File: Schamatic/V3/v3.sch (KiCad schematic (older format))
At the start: 29 parts, among them J1 SWD, J2 SENSOR, J3 CAN, Q1 PSMN014-40YS, Q2 PSMN014-40YS, Q3 PSMN014-40YS, Q4 PSMN014-40YS, Q5 PSMN014-40YS, Q6 PSMN014-40YS, U1 STSPIN32F0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

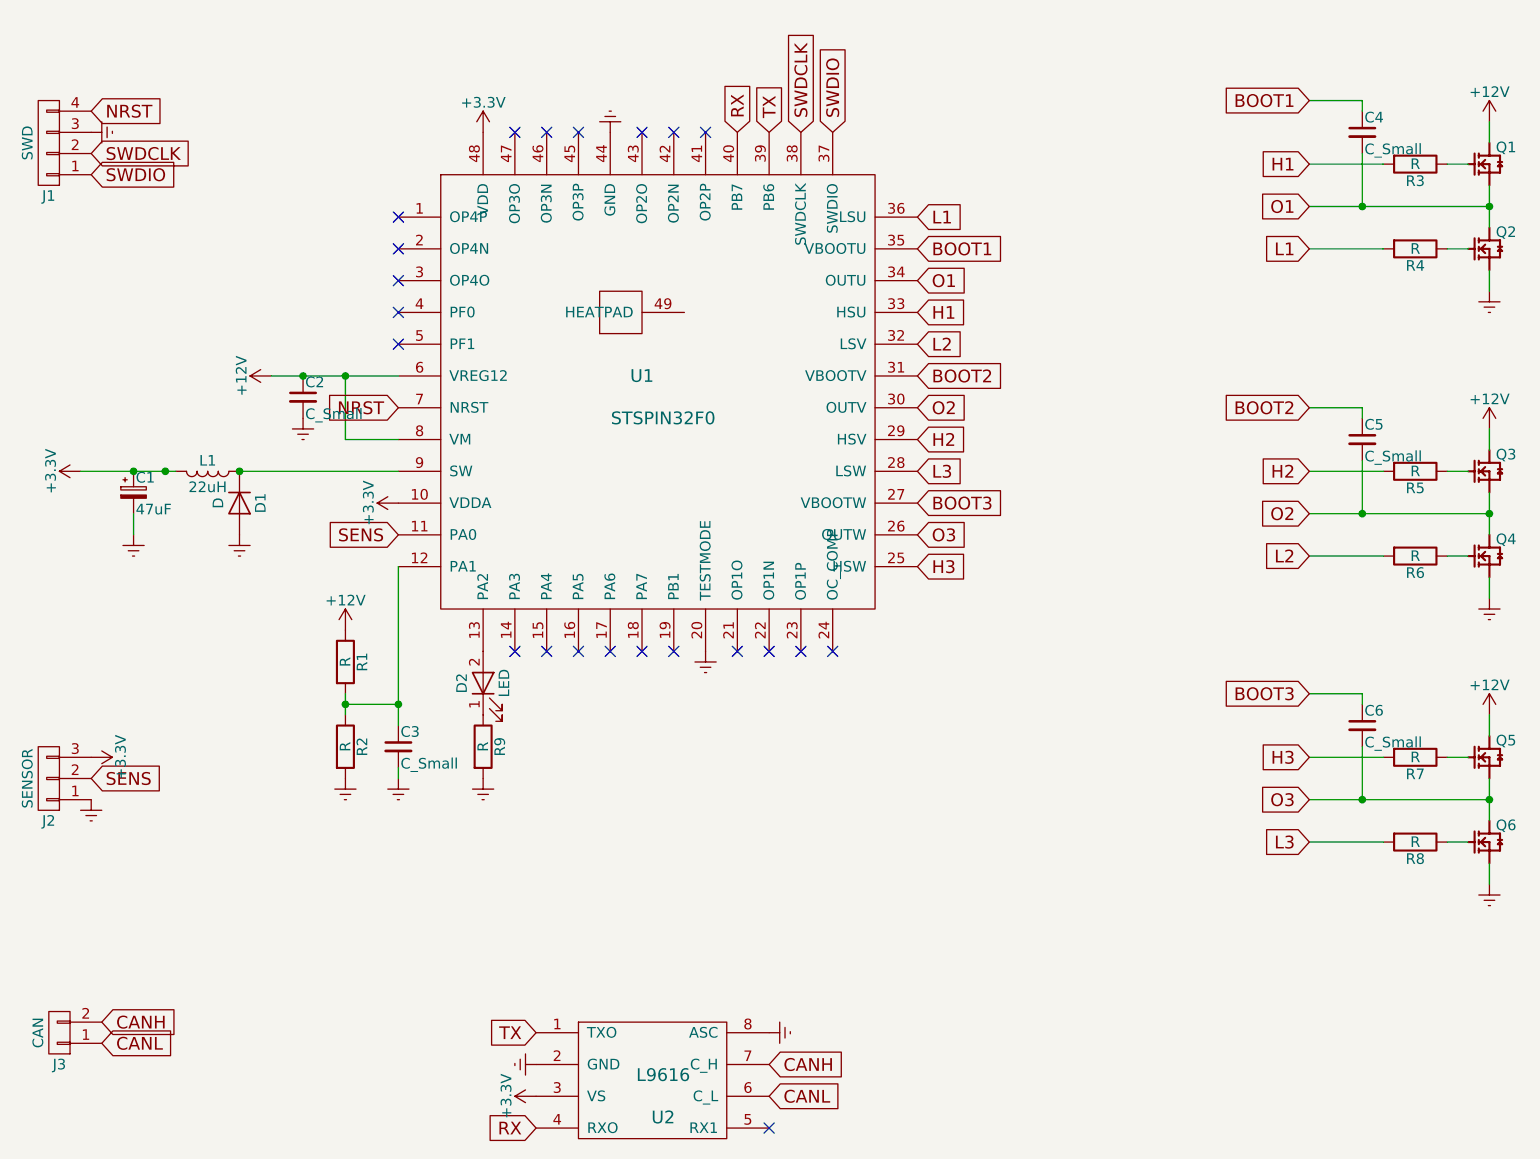
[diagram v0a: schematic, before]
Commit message: board ordered
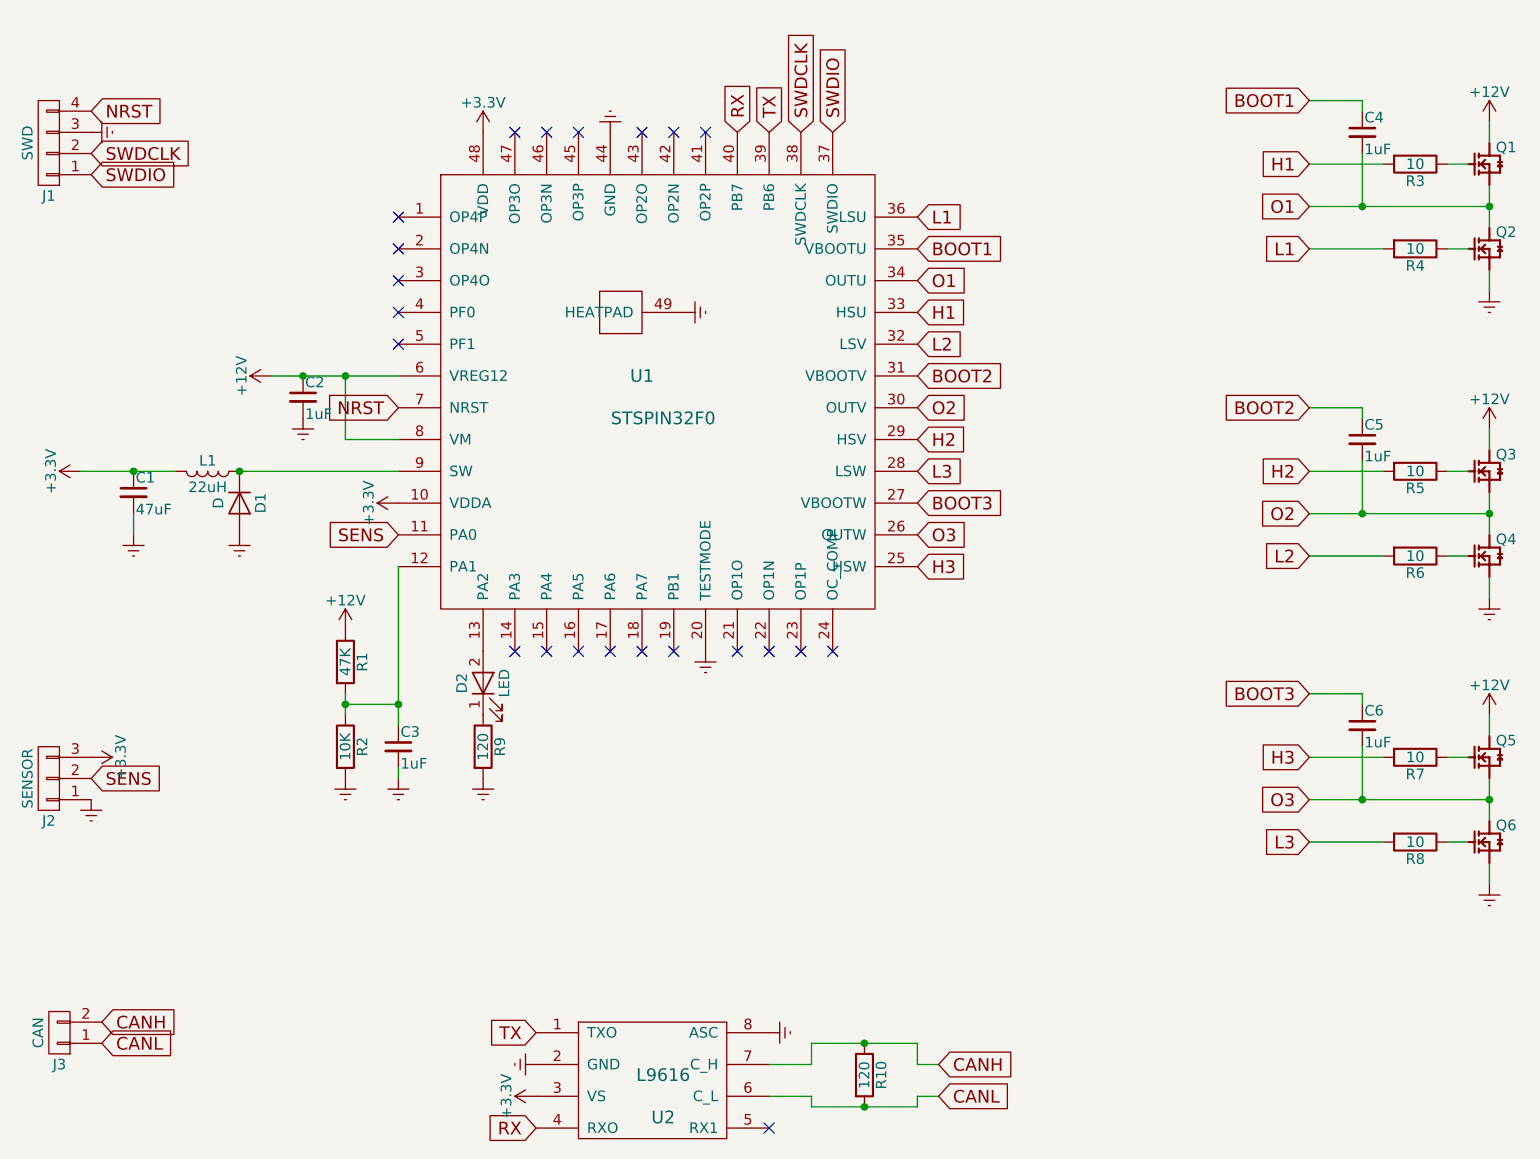
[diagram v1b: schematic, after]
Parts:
- removed C1: 47uF, Capacitors_SMD:CP_Elec_4x4.5, symbol CP_Small
- added C1: 47uF, Capacitors_SMD:C_0805, symbol C_Small
- added R10: 120, Resistors_SMD:R_0805_HandSoldering, symbol R
- C2, C3, C4, C5, C6: value C_Small -> 1uF
- L1: footprint Choke_SMD:Choke_SMD_6.3x6.3_H3 -> Inductors_SMD:L_1812
- Q1, Q2, Q3, Q4, Q5, Q6: value PSMN014-40YS -> PSMN3R3-40YS
- R1: value R -> 47K
- R2: value R -> 10K
- R3, R4, R5, R6, R7, R8: value R -> 10
- R9: value R -> 120
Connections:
- net +3V3: now also C1.1
- net CANH: now also R10.1
- net CANL: now also R10.2
- net Earth: now also U1.49 (HEATPAD), C1.2
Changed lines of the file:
@@
 LIBS:valves
 LIBS:Misha
+LIBS:v3-cache
 EELAYER 25 0
 EELAYER END
@@
 F 0 "L1" V 1700 3350 50  0000 C CNN
 F 1 "22uH" V 1825 3350 50  0000 C CNN
-F 2 "Choke_SMD:Choke_SMD_6.3x6.3_H3" H 1750 3350 50  0001 C CNN
+F 2 "Inductors_SMD:L_1812" H 1750 3350 50  0001 C CNN
 F 3 "" H 1750 3350 50  0001 C CNN
 	1    1750 3350
@@
 	1    1900 3500
 	0    1    1    0
-$EndComp
-$Comp
-L CP_Small C1
-U 1 1 597754B4
-P 1400 3450
-F 0 "C1" H 1410 3520 50  0000 L CNN
-F 1 "47uF" H 1410 3370 50  0000 L CNN
-F 2 "Capacitors_SMD:CP_Elec_4x4.5" H 1400 3450 50  0001 C CNN
-F 3 "" H 1400 3450 50  0001 C CNN
-	1    1400 3450
-	1    0    0    -1
 $EndComp
 $Comp
@@
 P 7800 2000
 F 0 "Q1" H 7830 2150 50  0000 L BNN
-F 1 "PSMN014-40YS" H 7800 2000 50  0001 L BNN
+F 1 "PSMN3R3-40YS" H 7800 2000 50  0001 L BNN
 F 2 "Misha:LFPAK" H 7800 2000 50  0001 L BNN
 F 3 "Good" H 7800 2000 50  0001 L BNN
@@
 P 7800 2400
 F 0 "Q2" H 7830 2550 50  0000 L BNN
-F 1 "PSMN014-40YS" H 7800 2400 50  0001 L BNN
+F 1 "PSMN3R3-40YS" H 7800 2400 50  0001 L BNN
 F 2 "Misha:LFPAK" H 7800 2400 50  0001 L BNN
 F 3 "Good" H 7800 2400 50  0001 L BNN
@@
 P 7450 1900
 F 0 "R3" V 7530 1900 50  0000 C CNN
-F 1 "R" V 7450 1900 50  0000 C CNN
+F 1 "10" V 7450 1900 50  0000 C CNN
 F 2 "Resistors_SMD:R_0805" V 7380 1900 50  0001 C CNN
 F 3 "" H 7450 1900 50  0001 C CNN
@@
 Wire Wire Line
 	1400 3650 1400 3550
-Connection ~ 1550 3350
 Wire Wire Line
 	7800 2200 7800 2000
@@
 P 7450 2300
 F 0 "R4" V 7530 2300 50  0000 C CNN
-F 1 "R" V 7450 2300 50  0000 C CNN
+F 1 "10" V 7450 2300 50  0000 C CNN
 F 2 "Resistors_SMD:R_0805" V 7380 2300 50  0001 C CNN
 F 3 "" H 7450 2300 50  0001 C CNN
@@
 P 7200 1750
 F 0 "C4" H 7210 1820 50  0000 L CNN
-F 1 "C_Small" H 7210 1670 50  0000 L CNN
+F 1 "1uF" H 7210 1670 50  0000 L CNN
 F 2 "Capacitors_SMD:C_0805" H 7200 1750 50  0001 C CNN
 F 3 "" H 7200 1750 50  0001 C CNN
@@
 	0    1    1    0
 $EndComp
-Text GLabel 4400 6150 2    60   Input ~ 0
+Text GLabel 5200 6150 2    60   Input ~ 0
 CANH
-Text GLabel 4400 6300 2    60   Input ~ 0
+Text GLabel 5200 6300 2    60   Input ~ 0
 CANL
 Text GLabel 1250 5950 2    60   Input ~ 0
@@
 P 2650 4650
 F 0 "C3" H 2660 4720 50  0000 L CNN
-F 1 "C_Small" H 2660 4570 50  0000 L CNN
+F 1 "1uF" H 2660 4570 50  0000 L CNN
 F 2 "Capacitors_SMD:C_0805" H 2650 4650 50  0001 C CNN
 F 3 "" H 2650 4650 50  0001 C CNN
@@
 P 2400 4650
 F 0 "R2" V 2480 4650 50  0000 C CNN
-F 1 "R" V 2400 4650 50  0000 C CNN
+F 1 "10K" V 2400 4650 50  0000 C CNN
 F 2 "Resistors_SMD:R_0805" V 2330 4650 50  0001 C CNN
 F 3 "" H 2400 4650 50  0001 C CNN
@@
 P 2400 4250
 F 0 "R1" V 2480 4250 50  0000 C CNN
-F 1 "R" V 2400 4250 50  0000 C CNN
+F 1 "47K" V 2400 4250 50  0000 C CNN
 F 2 "Resistors_SMD:R_0805" V 2330 4250 50  0001 C CNN
 F 3 "" H 2400 4250 50  0001 C CNN
@@
 P 2200 3000
 F 0 "C2" H 2210 3070 50  0000 L CNN
-F 1 "C_Small" H 2210 2920 50  0000 L CNN
+F 1 "1uF" H 2210 2920 50  0000 L CNN
 F 2 "Capacitors_SMD:C_0805" H 2200 3000 50  0001 C CNN
 F 3 "" H 2200 3000 50  0001 C CNN
@@
 P 7800 3450
 F 0 "Q3" H 7830 3600 50  0000 L BNN
-F 1 "PSMN014-40YS" H 7800 3450 50  0001 L BNN
+F 1 "PSMN3R3-40YS" H 7800 3450 50  0001 L BNN
 F 2 "Misha:LFPAK" H 7800 3450 50  0001 L BNN
 F 3 "Good" H 7800 3450 50  0001 L BNN
@@
 P 7800 3850
 F 0 "Q4" H 7830 4000 50  0000 L BNN
-F 1 "PSMN014-40YS" H 7800 3850 50  0001 L BNN
+F 1 "PSMN3R3-40YS" H 7800 3850 50  0001 L BNN
 F 2 "Misha:LFPAK" H 7800 3850 50  0001 L BNN
 F 3 "Good" H 7800 3850 50  0001 L BNN
@@
 P 7450 3350
 F 0 "R5" V 7530 3350 50  0000 C CNN
-F 1 "R" V 7450 3350 50  0000 C CNN
+F 1 "10" V 7450 3350 50  0000 C CNN
 F 2 "Resistors_SMD:R_0805" V 7380 3350 50  0001 C CNN
 F 3 "" H 7450 3350 50  0001 C CNN
@@
 P 7450 3750
 F 0 "R6" V 7530 3750 50  0000 C CNN
-F 1 "R" V 7450 3750 50  0000 C CNN
+F 1 "10" V 7450 3750 50  0000 C CNN
 F 2 "Resistors_SMD:R_0805" V 7380 3750 50  0001 C CNN
 F 3 "" H 7450 3750 50  0001 C CNN
@@
 P 7200 3200
 F 0 "C5" H 7210 3270 50  0000 L CNN
-F 1 "C_Small" H 7210 3120 50  0000 L CNN
+F 1 "1uF" H 7210 3120 50  0000 L CNN
 F 2 "Capacitors_SMD:C_0805" H 7200 3200 50  0001 C CNN
 F 3 "" H 7200 3200 50  0001 C CNN
@@
 P 7800 4800
 F 0 "Q5" H 7830 4950 50  0000 L BNN
-F 1 "PSMN014-40YS" H 7800 4800 50  0001 L BNN
+F 1 "PSMN3R3-40YS" H 7800 4800 50  0001 L BNN
 F 2 "Misha:LFPAK" H 7800 4800 50  0001 L BNN
 F 3 "Good" H 7800 4800 50  0001 L BNN
@@
 P 7800 5200
 F 0 "Q6" H 7830 5350 50  0000 L BNN
-F 1 "PSMN014-40YS" H 7800 5200 50  0001 L BNN
+F 1 "PSMN3R3-40YS" H 7800 5200 50  0001 L BNN
 F 2 "Misha:LFPAK" H 7800 5200 50  0001 L BNN
 F 3 "Good" H 7800 5200 50  0001 L BNN
@@
 P 7450 4700
 F 0 "R7" V 7530 4700 50  0000 C CNN
-F 1 "R" V 7450 4700 50  0000 C CNN
+F 1 "10" V 7450 4700 50  0000 C CNN
 F 2 "Resistors_SMD:R_0805" V 7380 4700 50  0001 C CNN
 F 3 "" H 7450 4700 50  0001 C CNN
@@
 P 7450 5100
 F 0 "R8" V 7530 5100 50  0000 C CNN
-F 1 "R" V 7450 5100 50  0000 C CNN
+F 1 "10" V 7450 5100 50  0000 C CNN
 F 2 "Resistors_SMD:R_0805" V 7380 5100 50  0001 C CNN
 F 3 "" H 7450 5100 50  0001 C CNN
@@
 P 7200 4550
 F 0 "C6" H 7210 4620 50  0000 L CNN
-F 1 "C_Small" H 7210 4470 50  0000 L CNN
+F 1 "1uF" H 7210 4470 50  0000 L CNN
 F 2 "Capacitors_SMD:C_0805" H 7200 4550 50  0001 C CNN
 F 3 "" H 7200 4550 50  0001 C CNN
@@
 P 3050 4650
 F 0 "R9" V 3130 4650 50  0000 C CNN
-F 1 "R" V 3050 4650 50  0000 C CNN
+F 1 "120" V 3050 4650 50  0000 C CNN
 F 2 "Resistors_SMD:R_0805" V 2980 4650 50  0001 C CNN
 F 3 "" H 3050 4650 50  0001 C CNN
@@
 NoConn ~ 4550 4200
 NoConn ~ 4700 4200
+$Comp
+L R R10
+U 1 1 5979C6A0
+P 4850 6200
+F 0 "R10" V 4930 6200 50  0000 C CNN
+F 1 "120" V 4850 6200 50  0000 C CNN
+F 2 "Resistors_SMD:R_0805_HandSoldering" V 4780 6200 50  0001 C CNN
+F 3 "" H 4850 6200 50  0001 C CNN
+	1    4850 6200
+	1    0    0    -1
+$EndComp
+Wire Wire Line
+	4400 6150 4600 6150
+Wire Wire Line
+	4600 6150 4600 6050
+Wire Wire Line
+	4600 6050 5100 6050
+Wire Wire Line
+	5100 6050 5100 6150
+Wire Wire Line
+	5100 6150 5200 6150
+Wire Wire Line
+	5200 6300 5100 6300
+Wire Wire Line
+	5100 6300 5100 6350
+Wire Wire Line
+	5100 6350 4600 6350
+Wire Wire Line
+	4600 6350 4600 6300
+Wire Wire Line
+	4600 6300 4400 6300
+Connection ~ 4850 6050
+Connection ~ 4850 6350
+$Comp
+L C_Small C1
+U 1 1 597BE295
+P 1400 3450
+F 0 "C1" H 1410 3520 50  0000 L CNN
+F 1 "47uF" H 1410 3370 50  0000 L CNN
+F 2 "Capacitors_SMD:C_0805" H 1400 3450 50  0001 C CNN
+F 3 "" H 1400 3450 50  0001 C CNN
+	1    1400 3450
+	1    0    0    -1
+$EndComp
+$Comp
+L Earth #PWR026
+U 1 1 597C6786
+P 4000 2600
+F 0 "#PWR026" H 4000 2350 50  0001 C CNN
+F 1 "Earth" H 4000 2450 50  0001 C CNN
+F 2 "" H 4000 2600 50  0001 C CNN
+F 3 "" H 4000 2600 50  0001 C CNN
+	1    4000 2600
+	0    -1   -1   0
+$EndComp
 $EndSCHEMATC
